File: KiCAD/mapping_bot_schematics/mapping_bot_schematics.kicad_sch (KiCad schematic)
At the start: 10 parts, among them M1 Motor_DC, M2 Motor_DC, U1 TB6612FNG, U2 HC-SR04

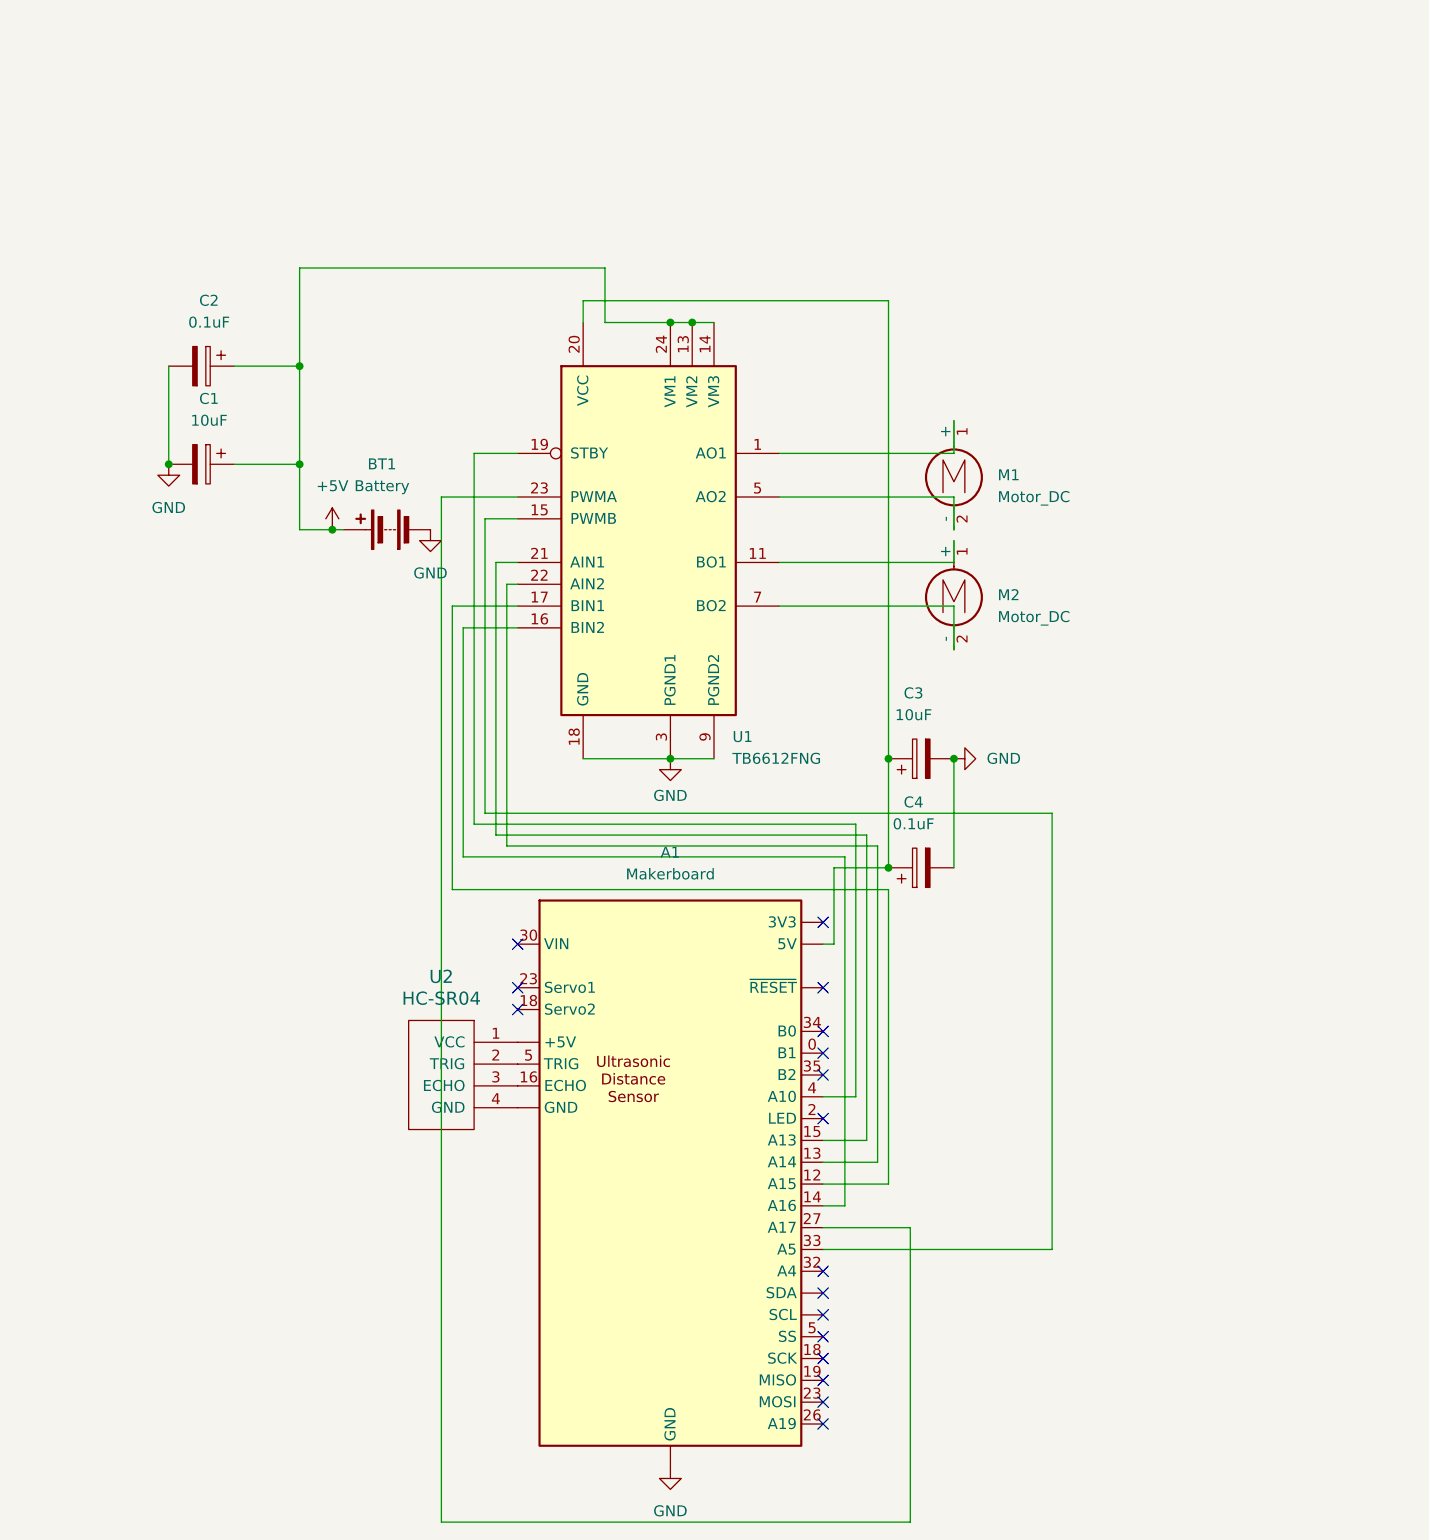
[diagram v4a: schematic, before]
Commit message: Add MPU6050 schematics update
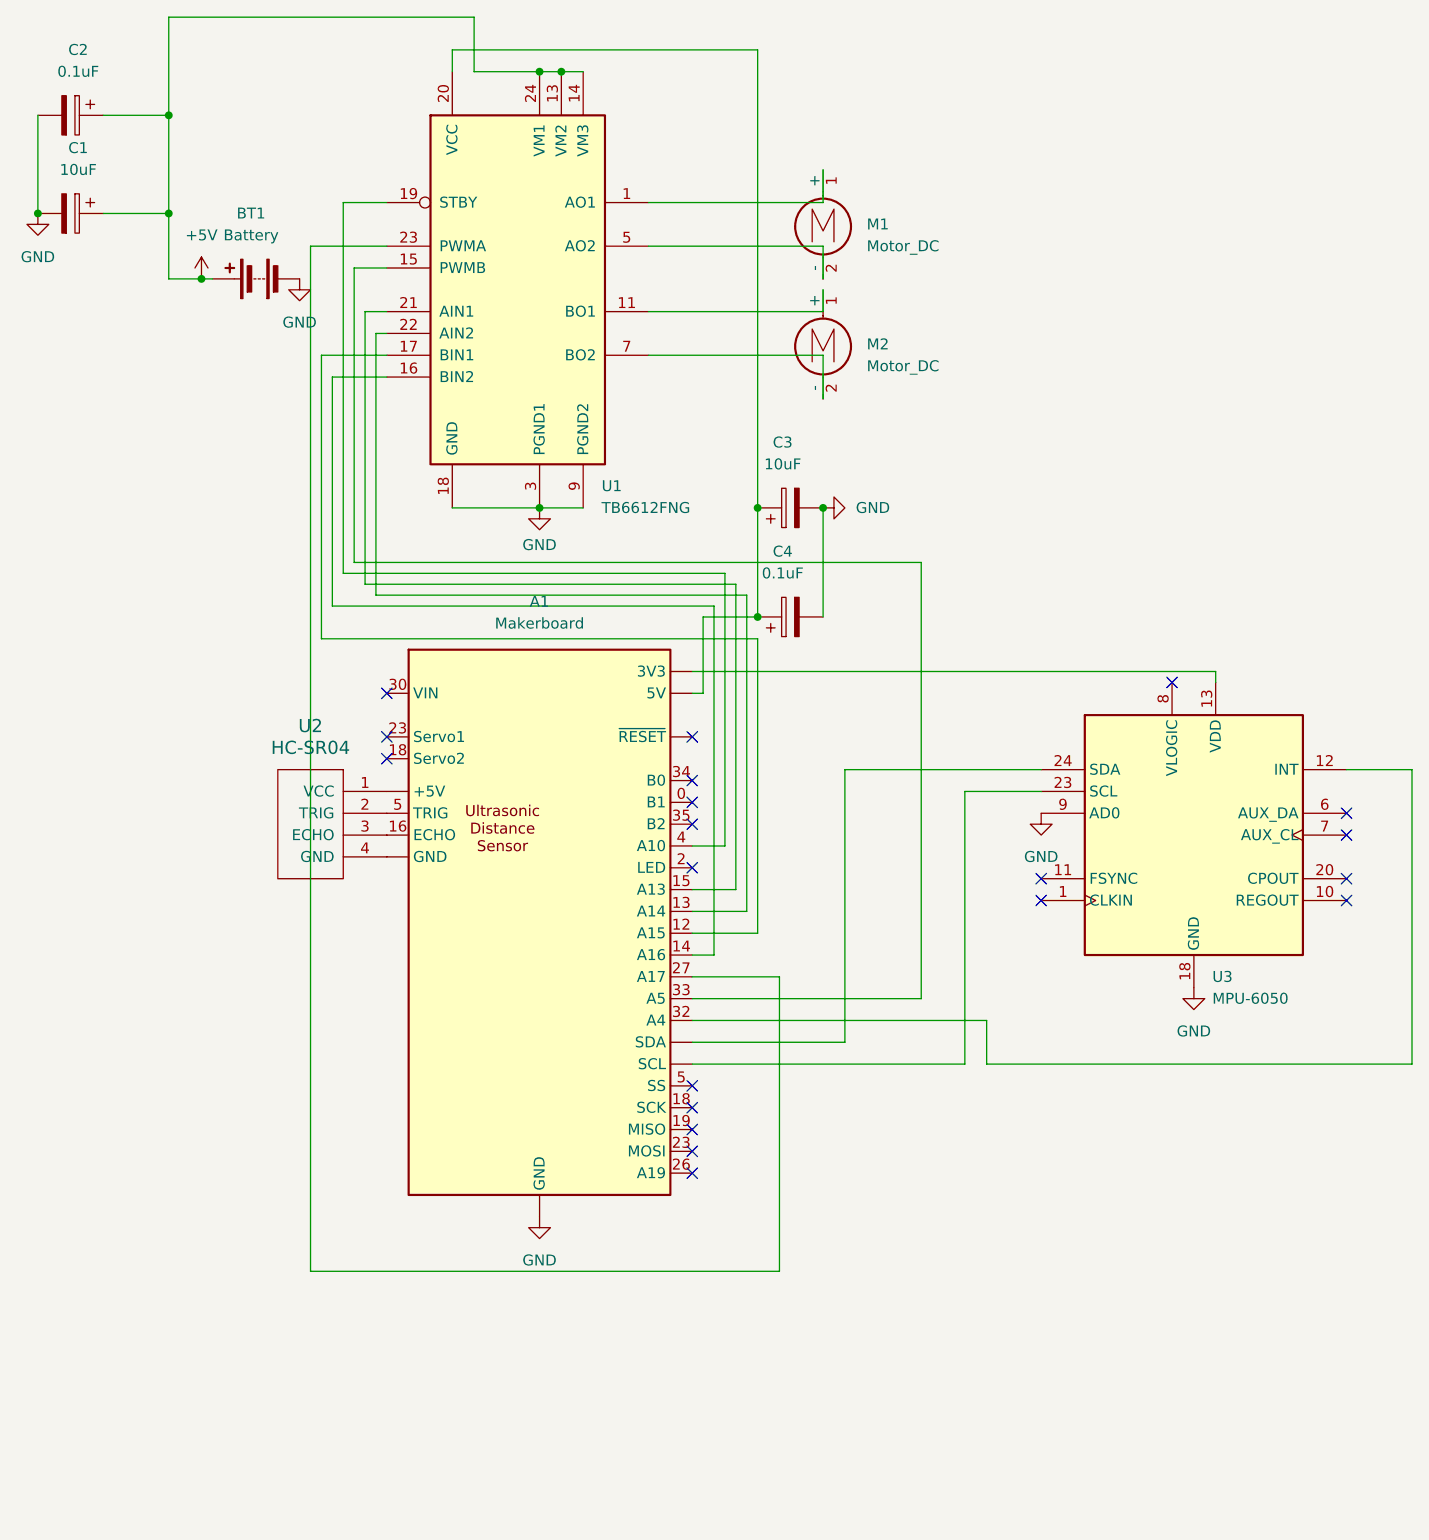
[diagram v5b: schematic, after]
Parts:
- added U3: MPU-6050, Sensor_Motion:InvenSense_QFN-24_4x4mm_P0.5mm, symbol Sensor_Motion:MPU-6050
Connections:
- net GND: now also U3.18 (GND), U3.9 (AD0)
- net at A1.32 (A4): now also U3.12 (INT)
- net at A1.5 (SS): now also U2.2 (TRIG)
- new net: A1. (SCL), U3.13 (VDD)
- new net: A1. (SCL), U3.23 (SCL)
- new net: A1. (SCL), U3.24 (SDA)
- no-connect marks 17 -> 20
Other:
- moved on the sheet: A1, BT1, C1, C2, C3, C4, M1, M2, U1, U2
